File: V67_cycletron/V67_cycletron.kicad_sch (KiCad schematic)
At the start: 41 parts, among them J1 USB_C_Receptacle_USB2.0_16P, U1 LM1117DT-5.0, U2 LM1117DT-3.3, U3 ESP32-S3-WROOM-1

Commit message: changed some stuff
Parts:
- removed IO1: Screw_Terminal_01x14, TerminalBlock:TerminalBlock_MaiXu_MX126-5.0-14P_1x14_P5.00mm, symbol Connector:Screw_Terminal_01x14
- removed vd1: 5023520400, Connector_4:CONN_SD-502352-001_04_MOL, symbol Connector_4:5023520400
- added IO1, IO2, IO3, IO4, voltage_divider_2con1: 5023520200, Connector_4:CONN_SD-502352-001_02_MOL, symbol Connector_2:5023520200
- added J3: Screw_Terminal_01x11, TerminalBlock:TerminalBlock_MaiXu_MX126-5.0-11P_1x11_P5.00mm, symbol Connector:Screw_Terminal_01x11
- added power5: Screw_Terminal_01x02, TerminalBlock:TerminalBlock_MaiXu_MX126-5.0-02P_1x02_P5.00mm, symbol Connector:Screw_Terminal_01x02
- vd_r1: footprint Resistor_SMD:R_0805_2012Metric_Pad1.20x1.40mm_HandSolder -> Resistor_THT:R_Axial_DIN0207_L6.3mm_D2.5mm_P7.62mm_Horizontal; LCSC C2933447 -> (none)
- renumbered power1 to power3
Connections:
- net PWM is gone; now on net Therm-: U3.21 (IO13)
- net +3.3V: now also voltage_divider_2con1.2
- net +5V: now also power5.1 (Pin_1)
- net GND: now also IO1.2, IO2.2, IO3.2, IO4.2, power5.2 (Pin_2)
- net I08: now also J3.11 (Pin_11)
- net I09: now also J3.10 (Pin_10)
- net I10: now also J3.9 (Pin_9)
- net I11: now also J3.8 (Pin_8)
- net I12: now also J3.7 (Pin_7)
- net I15: now also J3.6 (Pin_6)
- net I16: now also J3.5 (Pin_5)
- net I17: now also J3.4 (Pin_4)
- net I18: now also J3.3 (Pin_3)
- net I19: now also J3.2 (Pin_2)
- net IO4: now also IO1.1
- net IO5: now also IO2.1
- net IO6: now also IO3.1
- net IO7: now also IO4.1
- net Therm-: now also voltage_divider_2con1.1; no longer U3.20 (IO12)
- new net I20: J3.1 (Pin_1), U3.20 (IO12)
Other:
- moved on the sheet: vd_c2

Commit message: changed some stuff 2
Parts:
- removed input1: Screw_Terminal_01x02, TerminalBlock:TerminalBlock_MaiXu_MX126-5.0-02P_1x02_P5.00mm, symbol Connector:Screw_Terminal_01x02
- added D1, D2, D3: D_Schottky, Diode_SMD:D_SMA, symbol Device:D_Schottky
- added input1: 5023520200, Connector_4:CONN_SD-502352-001_02_MOL, symbol Connector_2:5023520200
- renumbered D1 to Dpower1
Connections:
- net +12V: now also D1.1 (K), D2.1 (K), D3.1 (K)
- net GND: now also input1.2
- net mosfet1_o: now also D1.2 (A)
- net mosfet2_o: now also D2.2 (A)
- net mosfet3_o: now also D3.2 (A)
- net at Dpower1.2 (A): now also input1.1
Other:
- moved on the sheet: Dpower1

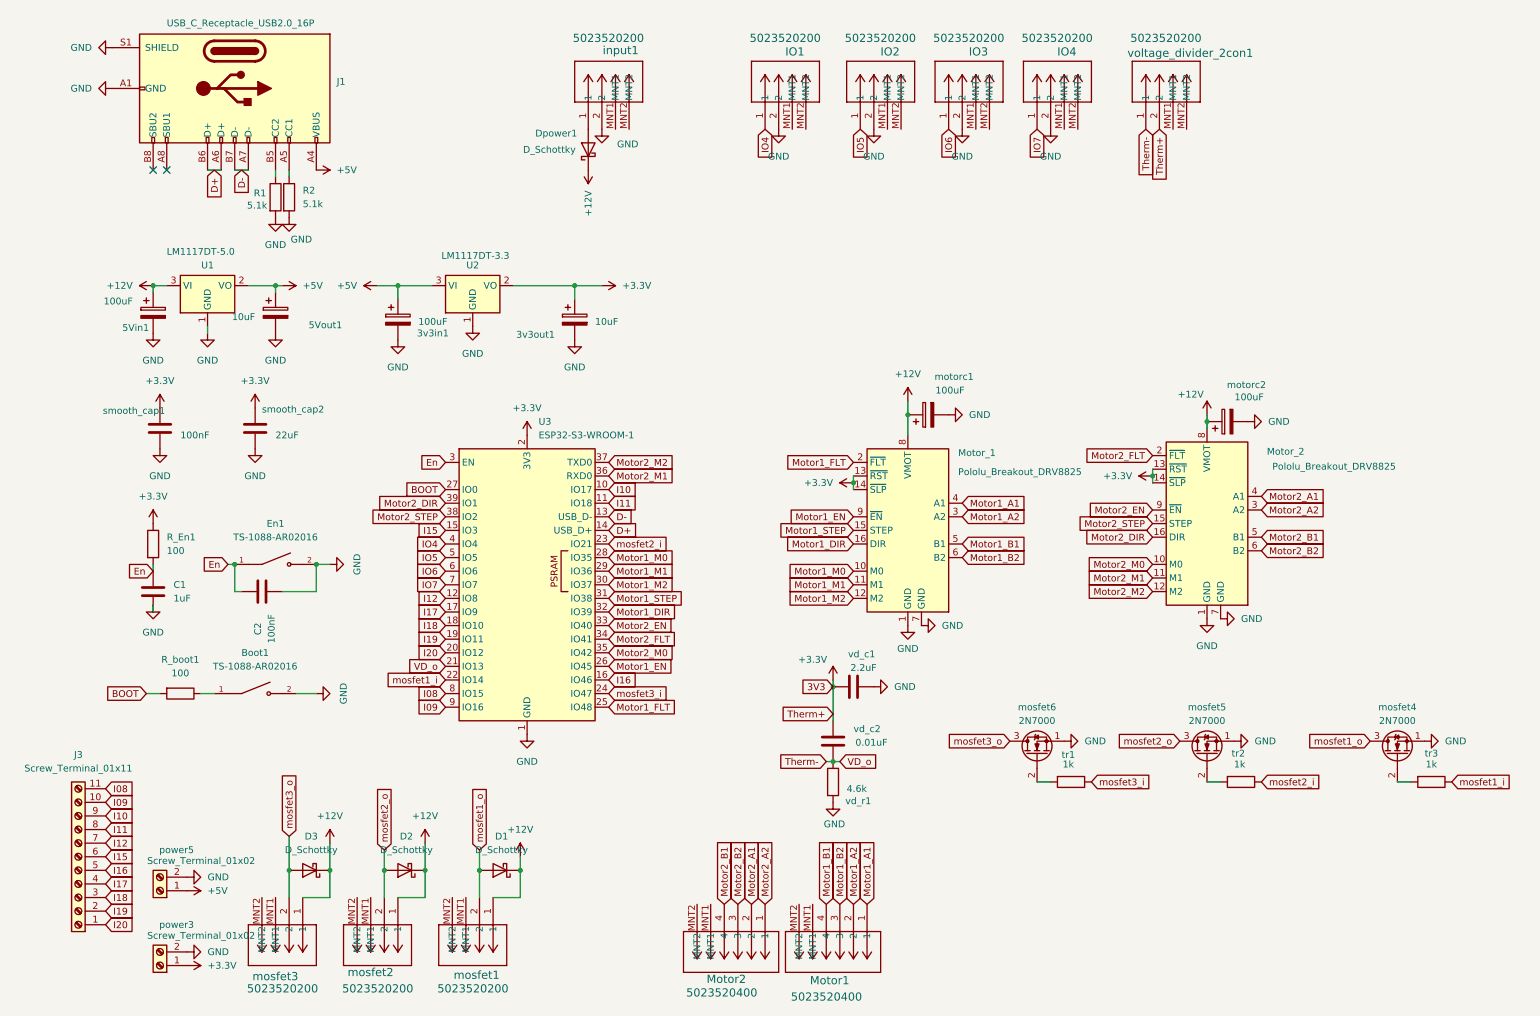
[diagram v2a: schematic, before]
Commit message: changed mosfets added more terminals
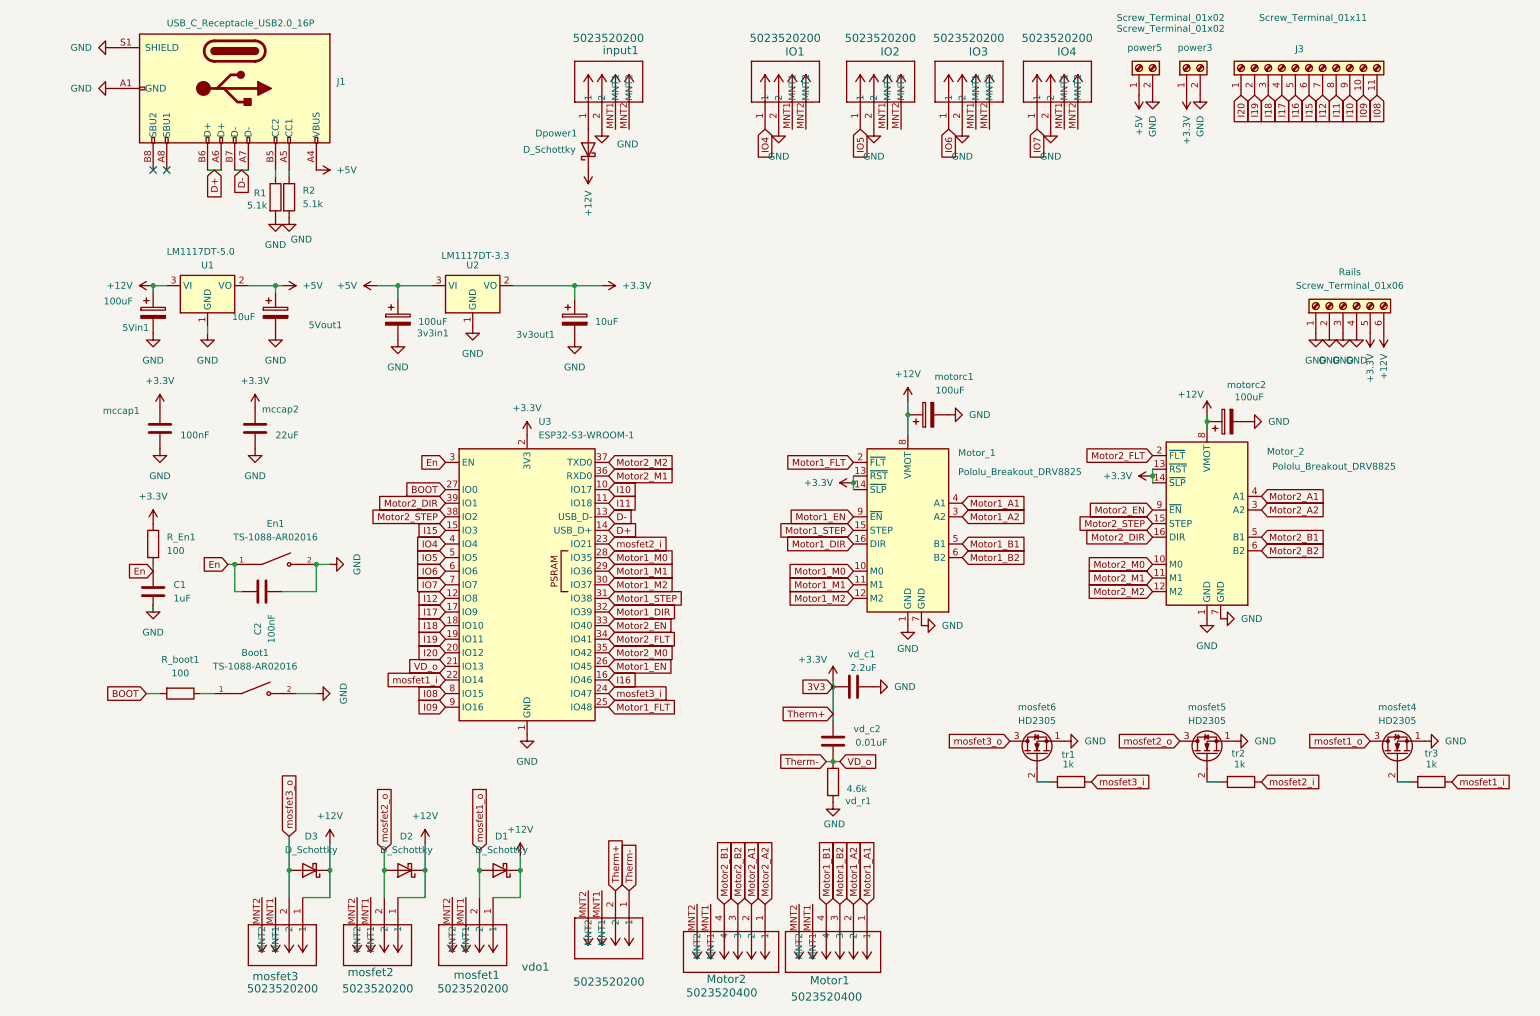
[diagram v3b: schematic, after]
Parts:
- added Rails: Screw_Terminal_01x06, TerminalBlock:TerminalBlock_MaiXu_MX126-5.0-06P_1x06_P5.00mm, symbol Connector:Screw_Terminal_01x06
- mosfet4, mosfet5, mosfet6: value 2N7000 -> HD2305; footprint Package_TO_SOT_THT:TO-92_Inline_Wide -> Package_TO_SOT_SMD:SOT-23; LCSC C9114 -> C466664
- renumbered smooth_cap1 to mccap1, smooth_cap2 to mccap2, voltage_divider_2con1 to vdo1
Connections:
- net +12V: now also Rails.6 (Pin_6)
- net +3.3V: now also Rails.5 (Pin_5)
- net GND: now also Rails.1 (Pin_1), Rails.2 (Pin_2), Rails.3 (Pin_3), Rails.4 (Pin_4)
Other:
- moved on the sheet: J3, power3, power5, vdo1

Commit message: fixed drc, added silscreen notes, made certain vias bigger
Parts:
- removed U3: ESP32-S3-WROOM-1, RF_Module:ESP32-S3-WROOM-1, symbol RF_Module:ESP32-S3-WROOM-1
- added U4: ESP32-S3-WROOM-1, RF_Module:ESP32-S3-WROOM-1, symbol RF_Module:ESP32-S3-WROOM-1
- renumbered Rails to Rails1
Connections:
- net +3.3V: now also U4.2 (3V3)
- net BOOT: now also U4.27 (IO0)
- net D+: now also U4.14 (USB_D+)
- net D-: now also U4.13 (USB_D-)
- net En: now also U4.3 (EN)
- net GND: now also U4.1 (GND), U4.40 (GND), U4.41 (GND)
- net I08: now also U4.8 (IO15)
- net I09: now also U4.9 (IO16)
- net I10: now also U4.10 (IO17)
- net I11: now also U4.11 (IO18)
- net I12: now also U4.12 (IO8)
- net I15: now also U4.15 (IO3)
- net I16: now also U4.16 (IO46)
- net I17: now also U4.17 (IO9)
- net I18: now also U4.18 (IO10)
- net I19: now also U4.19 (IO11)
- net I20: now also U4.20 (IO12)
- net IO4: now also U4.4 (IO4)
- net IO5: now also U4.5 (IO5)
- net IO6: now also U4.6 (IO6)
- net IO7: now also U4.7 (IO7)
- net Motor1_DIR: now also U4.32 (IO39)
- net Motor1_EN: now also U4.26 (IO45)
- net Motor1_FLT: now also U4.25 (IO48)
- net Motor1_M0: now also U4.28 (IO35)
- net Motor1_M1: now also U4.29 (IO36)
- net Motor1_M2: now also U4.30 (IO37)
- net Motor1_STEP: now also U4.31 (IO38)
- net Motor2_DIR: now also U4.39 (IO1)
- net Motor2_EN: now also U4.33 (IO40)
- net Motor2_FLT: now also U4.34 (IO41)
- net Motor2_M0: now also U4.35 (IO42)
- net Motor2_M1: now also U4.36 (RXD0)
- net Motor2_M2: now also U4.37 (TXD0)
- net Motor2_STEP: now also U4.38 (IO2)
- net Therm-: now also U4.21 (IO13)
- net mosfet1_i: now also U4.22 (IO14)
- net mosfet2_i: now also U4.23 (IO21)
- net mosfet3_i: now also U4.24 (IO47)
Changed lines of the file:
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@@
 		(dnp no)
 		(fields_autoplaced yes)
-		(property "Reference" "Rails"
+		(property "Reference" "Rails1"
 			(at 252.73 60.96 90)
 			(effects
@@
 			(project ""
 				(path "/490d8b32-3aea-4f11-93e7-a546853a1b13"
-					(reference "Rails")
+					(reference "Rails1")
 					(unit 1)
 				)
@@
 	)
 	(symbol
+		(lib_id "RF_Module:ESP32-S3-WROOM-1")
+		(at 99.06 119.38 0)
+		(unit 1)
+		(exclude_from_sim no)
+		(in_bom yes)
+		(on_board yes)
+		(dnp no)
+		(fields_autoplaced yes)
+		(property "Reference" "U4"
+			(at 101.2033 88.9 0)
+			(effects
+				(font
+					(size 1.27 1.27)
+				)
+				(justify left)
+			)
+		)
+		(property "Value" "ESP32-S3-WROOM-1"
+			(at 101.2033 91.44 0)
+			(effects
+				(font
+					(size 1.27 1.27)
+				)
+				(justify left)
+			)
+		)
+		(property "Footprint" "RF_Module:ESP32-S3-WROOM-1"
+			(at 99.06 116.84 0)
+			(effects
+				(font
+					(size 1.27 1.27)
+				)
+				(hide yes)
+			)
+		)
+		(property "Datasheet" "https://www.espressif.com/sites/default/files/documentation/esp32-s3-wroom-1_wroom-1u_datasheet_en.pdf"
+			(at 99.06 119.38 0)
+			(effects
+				(font
+					(size 1.27 1.27)
+				)
+				(hide yes)
+			)
+		)
+		(property "Description" "RF Module, ESP32-S3 SoC, Wi-Fi 802.11b/g/n, Bluetooth, BLE, 32-bit, 3.3V, onboard antenna, SMD"
+			(at 99.06 119.38 0)
+			(effects
+				(font
+					(size 1.27 1.27)
+				)
+				(hide yes)
+			)
+		)
+		(pin "22"
+		)
+		(pin "1"
+		)
+		(pin "41"
+		)
+		(pin "9"
+		)
+		(pin "8"
+		)
+		(pin "2"
+		)
+		(pin "40"
+		)
+		(pin "37"
+		)
+		(pin "15"
+		)
+		(pin "12"
+		)
+		(pin "39"
+		)
+		(pin "3"
+		)
+		(pin "27"
+		)
+		(pin "38"
+		)
+		(pin "4"
+		)
+		(pin "5"
+		)
+		(pin "6"
+		)
+		(pin "7"
+		)
+		(pin "17"
+		)
+		(pin "18"
+		)
+		(pin "19"
+		)
+		(pin "20"
+		)
+		(pin "21"
+		)
+		(pin "36"
+		)
+		(pin "14"
+		)
+		(pin "10"
+		)
+		(pin "23"
+		)
+		(pin "11"
+		)
+		(pin "34"
+		)
+		(pin "33"
+		)
+		(pin "28"
+		)
+		(pin "29"
+		)
+		(pin "31"
+		)
+		(pin "13"
+		)
+		(pin "35"
+		)
+		(pin "26"
+		)
+		(pin "24"
+		)
+		(pin "25"
+		)
+		(pin "32"
+		)
+		(pin "16"
+		)
+		(pin "30"
+		)
+		(instances
+			(project ""
+				(path "/490d8b32-3aea-4f11-93e7-a546853a1b13"
+					(reference "U4")
+					(unit 1)
+				)
+			)
+		)
+	)
+	(symbol
 		(lib_id "power:GND")
 		(at 52.07 50.8 0)
@@
 					(unit 1)
 				)
-			)
-		)
-	)
-	(symbol
-		(lib_id "RF_Module:ESP32-S3-WROOM-1")
-		(at 99.06 119.38 0)
-		(unit 1)
-		(exclude_from_sim no)
-		(in_bom yes)
-		(on_board yes)
-		(dnp no)
-		(fields_autoplaced yes)
-		(property "Reference" "U3"
-			(at 101.2033 88.9 0)
-			(effects
-				(font
-					(size 1.27 1.27)
-				)
-				(justify left)
-			)
-		)
-		(property "Value" "ESP32-S3-WROOM-1"
-			(at 101.2033 91.44 0)
-			(effects
-				(font
-					(size 1.27 1.27)
-				)
-				(justify left)
-			)
-		)
-		(property "Footprint" "RF_Module:ESP32-S3-WROOM-1"
-			(at 99.06 116.84 0)
-			(effects
-				(font
-					(size 1.27 1.27)
-				)
-				(hide yes)
-			)
-		)
-		(property "Datasheet" "https://www.espressif.com/sites/default/files/documentation/esp32-s3-wroom-1_wroom-1u_datasheet_en.pdf"
-			(at 99.06 119.38 0)
-			(effects
-				(font
-					(size 1.27 1.27)
-				)
-				(hide yes)
-			)
-		)
-		(property "Description" "RF Module, ESP32-S3 SoC, Wi-Fi 802.11b/g/n, Bluetooth, BLE, 32-bit, 3.3V, onboard antenna, SMD"
-			(at 99.06 119.38 0)
-			(effects
-				(font
-					(size 1.27 1.27)
-				)
-				(hide yes)
-			)
-		)
-		(property "LCSC" "C2913197"
-			(at 101.2033 88.9 0)
-			(effects
-				(font
-					(size 1.27 1.27)
-				)
-				(hide yes)
-			)
-		)
-		(pin "12"
-		)
-		(pin "39"
-		)
-		(pin "38"
-		)
-		(pin "37"
-		)
-		(pin "11"
-		)
-		(pin "3"
-		)
-		(pin "27"
-		)
-		(pin "30"
-		)
-		(pin "15"
-		)
-		(pin "2"
-		)
-		(pin "20"
-		)
-		(pin "1"
-		)
-		(pin "41"
-		)
-		(pin "5"
-		)
-		(pin "21"
-		)
-		(pin "8"
-		)
-		(pin "4"
-		)
-		(pin "6"
-		)
-		(pin "9"
-		)
-		(pin "22"
-		)
-		(pin "10"
-		)
-		(pin "13"
-		)
-		(pin "40"
-		)
-		(pin "14"
-		)
-		(pin "7"
-		)
-		(pin "17"
-		)
-		(pin "18"
-		)
-		(pin "19"
-		)
-		(pin "36"
-		)
-		(pin "23"
-		)
-		(pin "28"
-		)
-		(pin "29"
-		)
-		(pin "33"
-		)
-		(pin "35"
-		)
-		(pin "24"
-		)
-		(pin "25"
-		)
-		(pin "32"
-		)
-		(pin "26"
-		)
-		(pin "31"
-		)
-		(pin "34"
-		)
-		(pin "16"
-		)
-		(instances
-			(project ""
-				(path "/490d8b32-3aea-4f11-93e7-a546853a1b13"
-					(reference "U3")
-					(unit 1)
-				)

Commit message: purchased boards
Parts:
- added D4, D5: LED, LED_SMD:LED_0603_1608Metric_Pad1.05x0.95mm_HandSolder, symbol Device:LED
- added R3: 1k, Resistor_SMD:R_0805_2012Metric_Pad1.20x1.40mm_HandSolder, symbol Device:R
- added R4: 4.7k, Resistor_SMD:R_0805_2012Metric_Pad1.20x1.40mm_HandSolder, symbol Device:R
- 3v3in1, 5Vin1: LCSC C2749 -> C7469933
- mccap2: Label C1711 -> C76634
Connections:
- net +12V: now also D5.2 (A)
- net +3.3V: now also D4.2 (A)
- net GND: now also R3.1, R4.1
- new net: D5.1 (K), R4.2
- new net: D4.1 (K), R3.2
